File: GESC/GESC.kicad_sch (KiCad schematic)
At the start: 0 parts

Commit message: aaaaaaaaaaaaaaaaaaa
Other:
- added sheet CAN (can.kicad_sch)
- added sheet Logic (Logic.kicad_sch)
- added sheet voltage regulation (regulators.kicad_sch)
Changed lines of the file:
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@@
 	(paper "A4")
+	(sheet
+		(at 64.77 73.66)
+		(size 48.26 36.83)
+		(fields_autoplaced yes)
+		(stroke
+			(width 0.1524)
+			(type solid)
+		)
+		(fill
+			(color 0 0 0 0.0000)
+		)
+		(property "Sheetname" "Logic"
+			(at 64.77 72.9484 0)
+			(effects
+				(font
+					(size 1.27 1.27)
+				)
+				(justify left bottom)
+			)
+		)
+		(property "Sheetfile" "Logic.kicad_sch"
+			(at 64.77 111.0746 0)
+			(effects
+				(font
+					(size 1.27 1.27)
+				)
+				(justify left top)
+			)
+		)
+		(instances
+			(project "GESC"
+				(path "/dc289c68-d15f-4833-9b73-29cf7cb2a289"
+					(page "3")
+				)
+			)
+		)
+	)
+	(sheet
+		(at 68.58 130.81)
+		(size 25.4 17.78)
+		(fields_autoplaced yes)
+		(stroke
+			(width 0.1524)
+			(type solid)
+		)
+		(fill
+			(color 0 0 0 0.0000)
+		)
+		(property "Sheetname" "CAN"
+			(at 68.58 130.0984 0)
+			(effects
+				(font
+					(size 1.27 1.27)
+				)
+				(justify left bottom)
+			)
+		)
+		(property "Sheetfile" "can.kicad_sch"
+			(at 68.58 149.1746 0)
+			(effects
+				(font
+					(size 1.27 1.27)
+				)
+				(justify left top)
+			)
+		)
+		(instances
+			(project "GESC"
+				(path "/dc289c68-d15f-4833-9b73-29cf7cb2a289"
+					(page "5")
+				)
+			)
+		)
+	)
+	(sheet
+		(at 41.91 34.29)
+		(size 24.13 19.05)
+		(fields_autoplaced yes)
+		(stroke
+			(width 0.1524)
+			(type solid)
+		)
+		(fill
+			(color 0 0 0 0.0000)
+		)
+		(property "Sheetname" "voltage regulation"
+			(at 41.91 33.5784 0)
+			(effects
+				(font
+					(size 1.27 1.27)
+				)
+				(justify left bottom)
+			)
+		)
+		(property "Sheetfile" "regulators.kicad_sch"
+			(at 41.91 53.9246 0)
+			(effects
+				(font
+					(size 1.27 1.27)
+				)
+				(justify left top)
+			)
+		)
+		(instances
+			(project "GESC"
+				(path "/dc289c68-d15f-4833-9b73-29cf7cb2a289"
+					(page "4")
+				)
+			)
+		)
+	)
 	(sheet
 		(at 175.26 74.93)

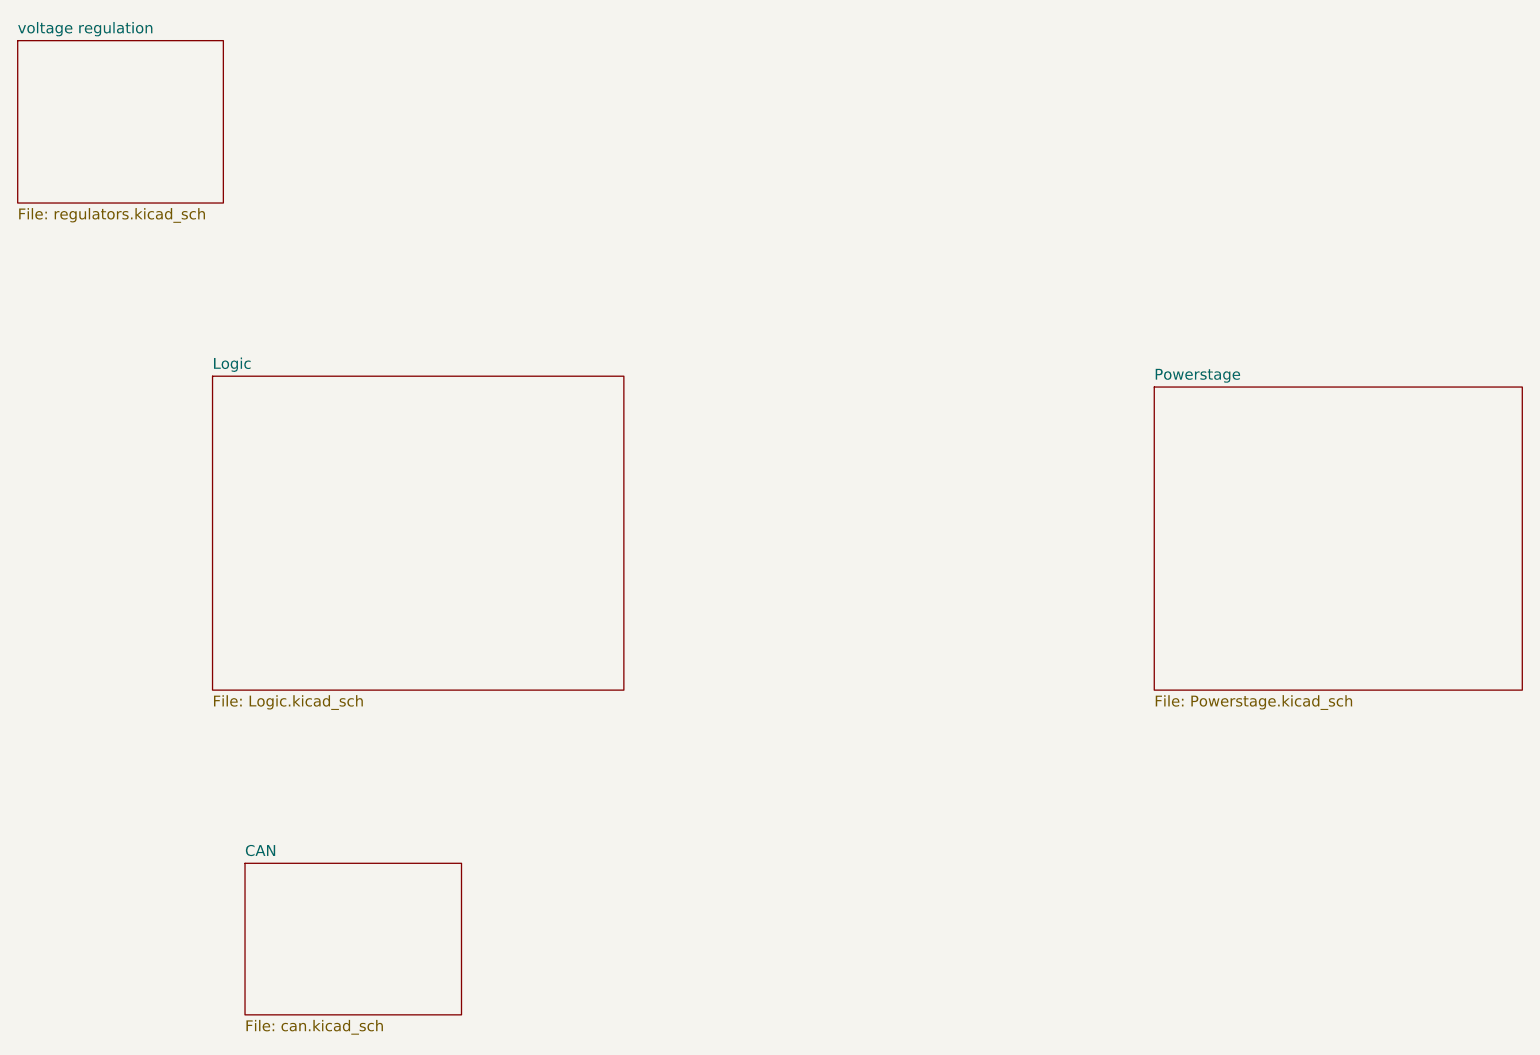
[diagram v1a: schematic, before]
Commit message: full to power board only
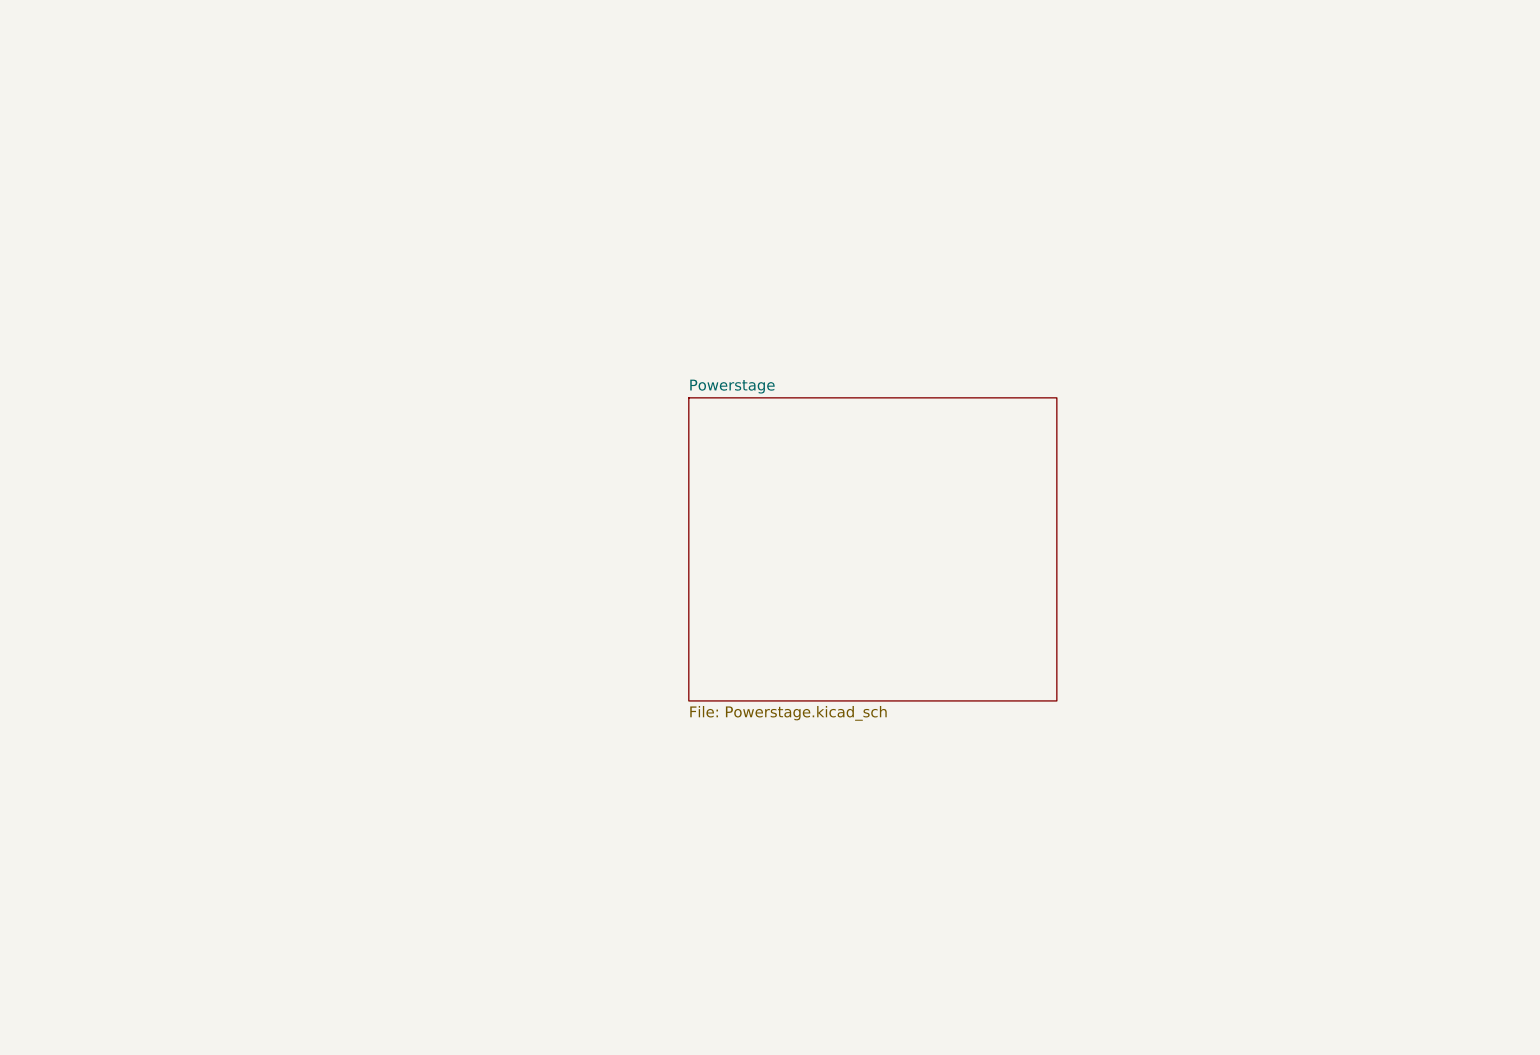
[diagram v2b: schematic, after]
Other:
- removed sheet CAN
- removed sheet Logic
- removed sheet voltage regulation
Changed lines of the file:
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@@
 	(paper "A4")
 	(sheet
-		(at 64.77 73.66)
-		(size 48.26 36.83)
-		(fields_autoplaced yes)
-		(stroke
-			(width 0.1524)
-			(type solid)
-		)
-		(fill
-			(color 0 0 0 0.0000)
-		)
-		(property "Sheetname" "Logic"
-			(at 64.77 72.9484 0)
-			(effects
-				(font
-					(size 1.27 1.27)
-				)
-				(justify left bottom)
-			)
-		)
-		(property "Sheetfile" "Logic.kicad_sch"
-			(at 64.77 111.0746 0)
-			(effects
-				(font
-					(size 1.27 1.27)
-				)
-				(justify left top)
-			)
-		)
-		(instances
-			(project "GESC"
-				(path "/dc289c68-d15f-4833-9b73-29cf7cb2a289"
-					(page "3")
-				)
-			)
-		)
-	)
-	(sheet
-		(at 68.58 130.81)
-		(size 25.4 17.78)
-		(fields_autoplaced yes)
-		(stroke
-			(width 0.1524)
-			(type solid)
-		)
-		(fill
-			(color 0 0 0 0.0000)
-		)
-		(property "Sheetname" "CAN"
-			(at 68.58 130.0984 0)
-			(effects
-				(font
-					(size 1.27 1.27)
-				)
-				(justify left bottom)
-			)
-		)
-		(property "Sheetfile" "can.kicad_sch"
-			(at 68.58 149.1746 0)
-			(effects
-				(font
-					(size 1.27 1.27)
-				)
-				(justify left top)
-			)
-		)
-		(instances
-			(project "GESC"
-				(path "/dc289c68-d15f-4833-9b73-29cf7cb2a289"
-					(page "5")
-				)
-			)
-		)
-	)
-	(sheet
-		(at 41.91 34.29)
-		(size 24.13 19.05)
-		(fields_autoplaced yes)
-		(stroke
-			(width 0.1524)
-			(type solid)
-		)
-		(fill
-			(color 0 0 0 0.0000)
-		)
-		(property "Sheetname" "voltage regulation"
-			(at 41.91 33.5784 0)
-			(effects
-				(font
-					(size 1.27 1.27)
-				)
-				(justify left bottom)
-			)
-		)
-		(property "Sheetfile" "regulators.kicad_sch"
-			(at 41.91 53.9246 0)
-			(effects
-				(font
-					(size 1.27 1.27)
-				)
-				(justify left top)
-			)
-		)
-		(instances
-			(project "GESC"
-				(path "/dc289c68-d15f-4833-9b73-29cf7cb2a289"
-					(page "4")
-				)
-			)
-		)
-	)
-	(sheet
-		(at 175.26 74.93)
+		(at 120.65 76.2)
 		(size 43.18 35.56)
 		(fields_autoplaced yes)
@@
 		)
 		(property "Sheetname" "Powerstage"
-			(at 175.26 74.2184 0)
+			(at 120.65 75.4884 0)
 			(effects
 				(font
@@
 		)
 		(property "Sheetfile" "Powerstage.kicad_sch"
-			(at 175.26 111.0746 0)
+			(at 120.65 112.3446 0)
 			(effects
 				(font
